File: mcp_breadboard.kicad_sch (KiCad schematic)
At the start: 32 parts, among them J1 VDD, J2 VDD, J3 GPIO, J4 UART/SPI, J5 USB_B_Micro, SW1 VDD_SEL, SW2 RST, SW3 SW_DIP_x04, U1 MCP2221AxSL, U2 MCP1826S

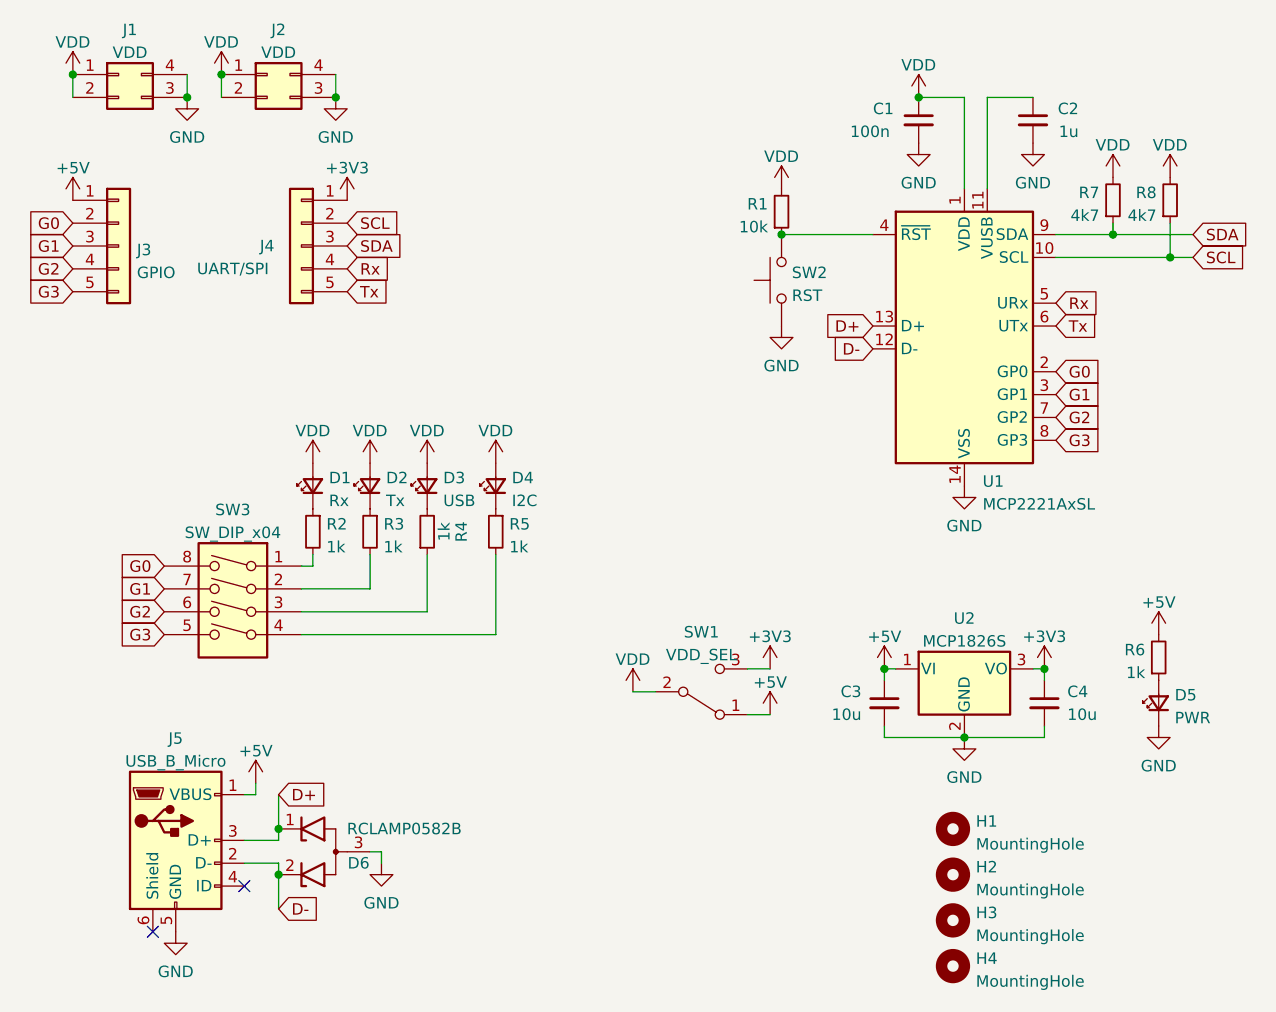
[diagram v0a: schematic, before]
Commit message: Final rev of design and layout, metrification of major board features for easier laser cutting.
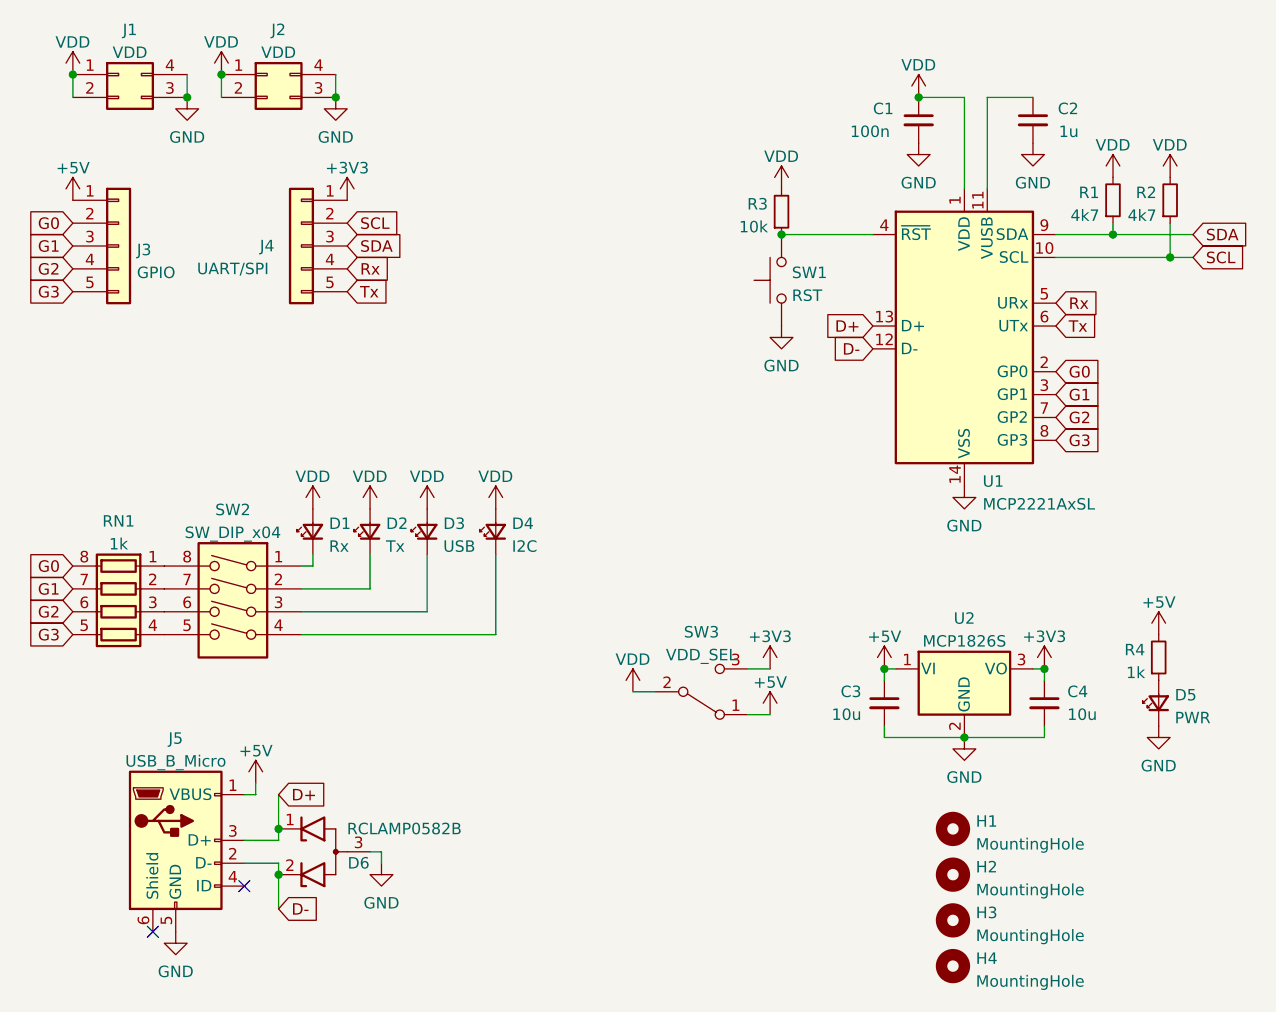
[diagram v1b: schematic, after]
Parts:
- removed R2, R3, R4, R5: 1k, Resistor_SMD:R_0603_1608Metric, symbol Device:R_Small
- added RN1: 1k, Resistor_SMD:R_Array_Convex_4x0603, symbol Device:R_Pack04
- renumbered R7 to R1, R8 to R2, R1 to R3, R6 to R4, SW2 to SW1, SW3 to SW2, SW1 to SW3
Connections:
- net G0: now also RN1.8 (R1.2); no longer SW2.8
- net G1: now also RN1.7 (R2.2); no longer SW2.7
- net G2: now also RN1.6 (R3.2); no longer SW2.6
- net G3: now also RN1.5 (R4.2); no longer SW2.5
- net at D4.1 (K): now also SW2.4
- net at D1.1 (K): now also SW2.1
- net at SW2.2: now also D2.1 (K)
- net at SW2.3: now also D3.1 (K)
- new net: RN1.4 (R4.1), SW2.5
- new net: RN1.3 (R3.1), SW2.6
- new net: RN1.2 (R2.1), SW2.7
- new net: RN1.1 (R1.1), SW2.8
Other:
- moved on the sheet: D1, D2, D3, D4

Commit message: extra part number
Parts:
- SW1: LCSC (none) -> C493020
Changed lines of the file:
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@@
+      (effects (font (size 1.27 1.27)) hide)
+    )
+    (property "LCSC" "C493020" (id 4) (at 97.79 45.72 90)
       (effects (font (size 1.27 1.27)) hide)
     )

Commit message: Final tweaks
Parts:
- C3, C4: LCSC (none) -> C1713
- D6: LCSC (none) -> C117553
- RN1: LCSC (none) -> C425239
- SW2: LCSC (none) -> C437204
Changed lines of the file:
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@@
+      (effects (font (size 1.27 1.27)) hide)
+    )
+    (property "LCSC" "C437204" (id 4) (at 36.83 82.55 0)
       (effects (font (size 1.27 1.27)) hide)
     )
@@
       (effects (font (size 1.27 1.27)) hide)
     )
+    (property "LCSC" "C1713" (id 4) (at 127 92.71 0)
+      (effects (font (size 1.27 1.27)) hide)
+    )
     (pin "1")
     (pin "2")
@@
       (effects (font (size 1.27 1.27)) hide)
     )
+    (property "LCSC" "C117553" (id 4) (at 46.99 109.22 0)
+      (effects (font (size 1.27 1.27)) hide)
+    )
     (pin "3")
     (pin "1")
@@
     )
     (property "Datasheet" "~" (id 3) (at 24.13 82.55 0)
+      (effects (font (size 1.27 1.27)) hide)
+    )
+    (property "LCSC" "C425239" (id 4) (at 24.13 82.55 0)
       (effects (font (size 1.27 1.27)) hide)
     )
@@
       (effects (font (size 1.27 1.27)) hide)
     )
+    (property "LCSC" "C1713" (id 4) (at 109.22 92.71 0)
+      (effects (font (size 1.27 1.27)) hide)
+    )

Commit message: Fix board outline for breadboard meshing.
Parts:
- H1, H2, H3, H4: footprint MountingHole:MountingHole_3.2mm_M3_ISO7380 -> MountingHole:MountingHole_2.7mm_M2.5_ISO7380
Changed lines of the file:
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@@
       (effects (font (size 1.27 1.27)) (justify left))
     )
-    (property "Footprint" "MountingHole:MountingHole_3.2mm_M3_ISO7380" (id 2) (at 116.84 121.92 0)
+    (property "Footprint" "MountingHole:MountingHole_2.7mm_M2.5_ISO7380" (id 2) (at 116.84 121.92 0)
       (effects (font (size 1.27 1.27)) hide)
     )
@@
       (effects (font (size 1.27 1.27)) (justify left))
     )
-    (property "Footprint" "MountingHole:MountingHole_3.2mm_M3_ISO7380" (id 2) (at 116.84 111.76 0)
+    (property "Footprint" "MountingHole:MountingHole_2.7mm_M2.5_ISO7380" (id 2) (at 116.84 111.76 0)
       (effects (font (size 1.27 1.27)) hide)
     )
@@
       (effects (font (size 1.27 1.27)) (justify left))
     )
-    (property "Footprint" "MountingHole:MountingHole_3.2mm_M3_ISO7380" (id 2) (at 116.84 116.84 0)
+    (property "Footprint" "MountingHole:MountingHole_2.7mm_M2.5_ISO7380" (id 2) (at 116.84 116.84 0)
       (effects (font (size 1.27 1.27)) hide)
     )
@@
       (effects (font (size 1.27 1.27)) (justify left))
     )
-    (property "Footprint" "MountingHole:MountingHole_3.2mm_M3_ISO7380" (id 2) (at 116.84 106.68 0)
+    (property "Footprint" "MountingHole:MountingHole_2.7mm_M2.5_ISO7380" (id 2) (at 116.84 106.68 0)
       (effects (font (size 1.27 1.27)) hide)
     )
@@
     )
     (path "/c3d0ffbb-456a-48d6-8a11-185c318af035"
-      (reference "H1") (unit 1) (value "MountingHole") (footprint "MountingHole:MountingHole_3.2mm_M3_ISO7380")
+      (reference "H1") (unit 1) (value "MountingHole") (footprint "MountingHole:MountingHole_2.7mm_M2.5_ISO7380")
     )
     (path "/1310b591-076c-4ed5-9a9d-c2e902776da3"
-      (reference "H2") (unit 1) (value "MountingHole") (footprint "MountingHole:MountingHole_3.2mm_M3_ISO7380")
+      (reference "H2") (unit 1) (value "MountingHole") (footprint "MountingHole:MountingHole_2.7mm_M2.5_ISO7380")
     )
     (path "/276c13a7-fe44-4453-aa73-fc5797ec36fc"
-      (reference "H3") (unit 1) (value "MountingHole") (footprint "MountingHole:MountingHole_3.2mm_M3_ISO7380")
+      (reference "H3") (unit 1) (value "MountingHole") (footprint "MountingHole:MountingHole_2.7mm_M2.5_ISO7380")
     )
     (path "/0c5027ba-4519-457a-a1d8-d50f528ae1e9"
-      (reference "H4") (unit 1) (value "MountingHole") (footprint "MountingHole:MountingHole_3.2mm_M3_ISO7380")
+      (reference "H4") (unit 1) (value "MountingHole") (footprint "MountingHole:MountingHole_2.7mm_M2.5_ISO7380")
     )
     (path "/fe148714-b0cf-44d7-9b6c-f06914620619"
